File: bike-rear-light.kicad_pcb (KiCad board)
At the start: 2 copper layers, 103.9 x 62.6 mm, 4 parts, among them U1 XT30PW-F

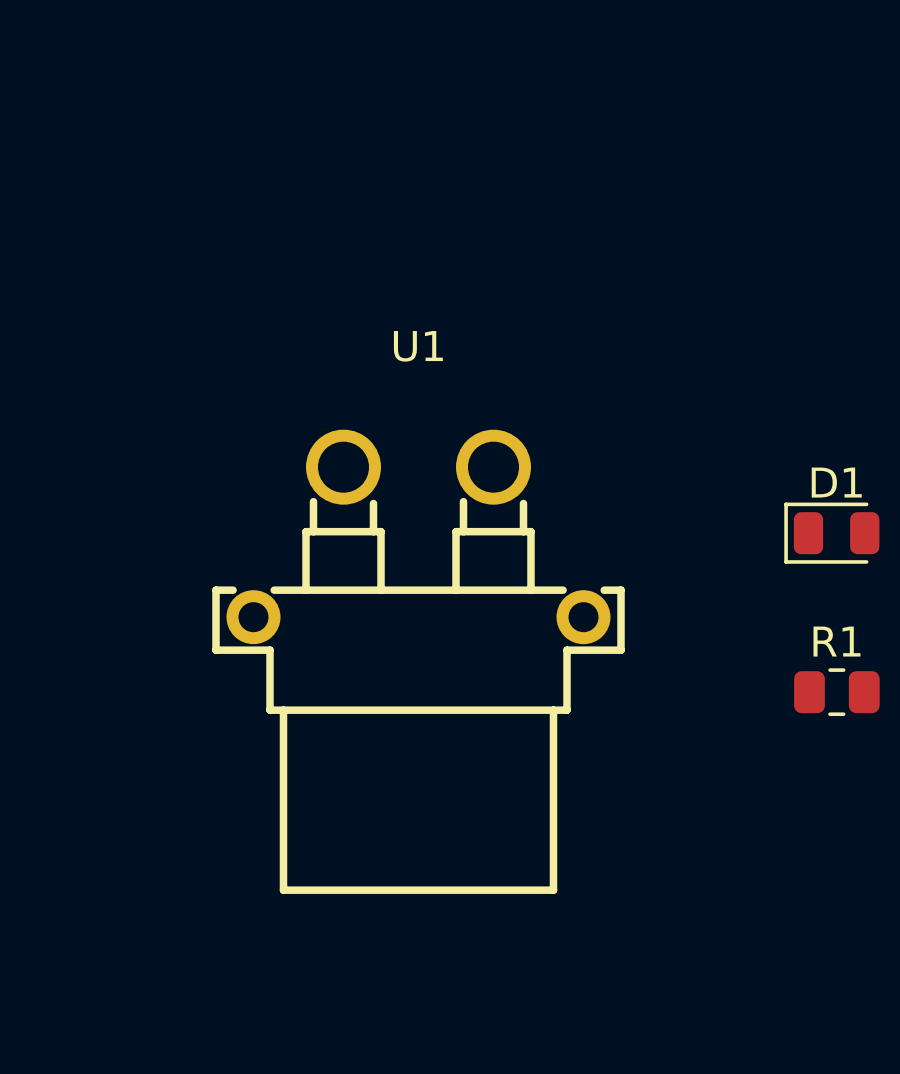
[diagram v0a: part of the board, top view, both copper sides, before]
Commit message: Moved power port
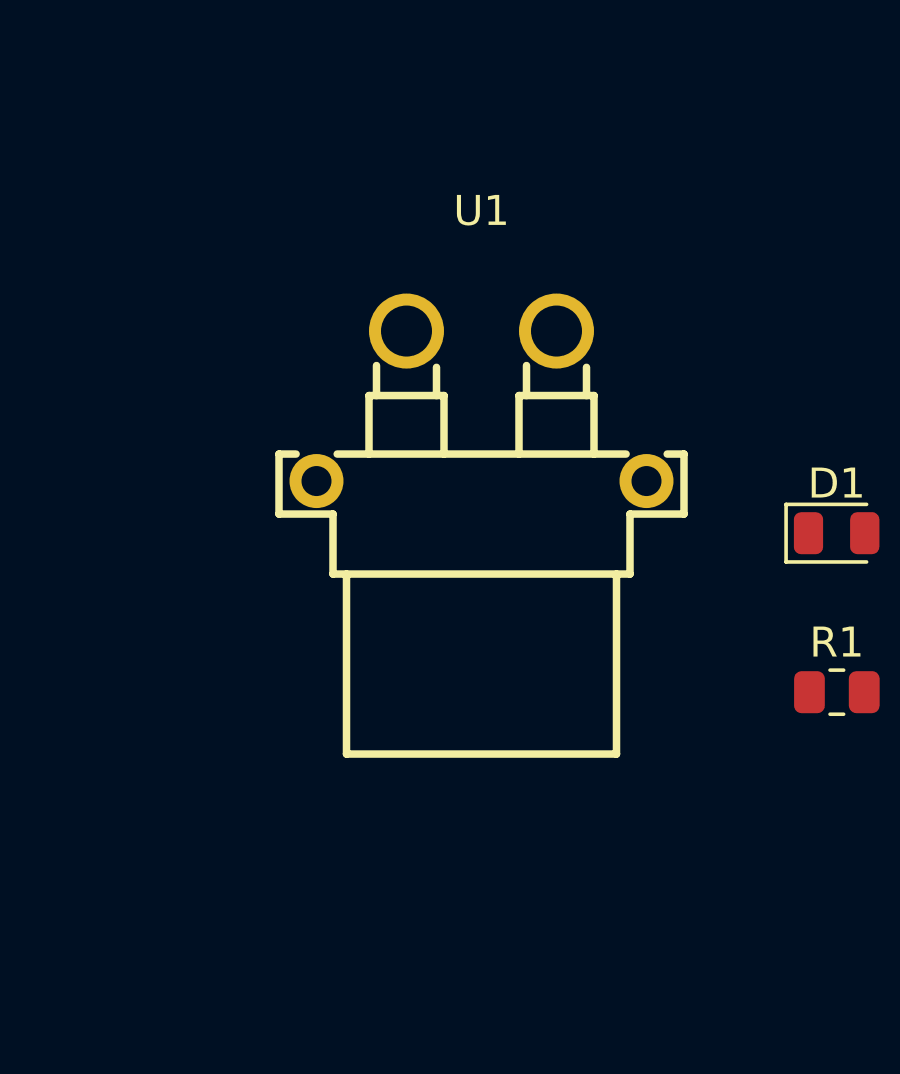
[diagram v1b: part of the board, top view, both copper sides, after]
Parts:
- moved U1 5.00 mm to (89.0, 71.8)
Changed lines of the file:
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@@
 	(footprint "easyeda2kicad:CONN-TH_XT30PW-F-1"
 		(layer "F.Cu")
-		(at 86.9 76.3)
+		(at 89 71.7625)
 		(property "Reference" "U1"
 			(at 0 -6.5 0)
